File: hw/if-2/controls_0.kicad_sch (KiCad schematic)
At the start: 17 parts, among them Q1 MMBT3904, Q13 2N7002, Q2 MMBT3904

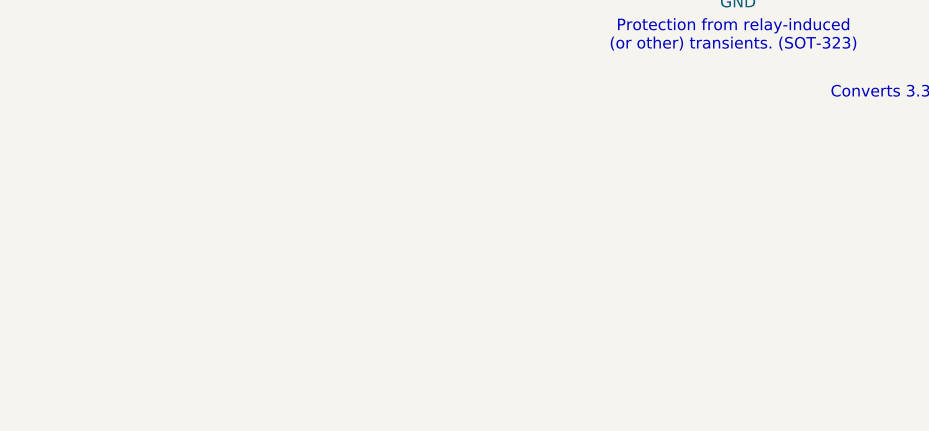
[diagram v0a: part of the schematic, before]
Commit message: Updating schematics, create new mini-board for radio interface
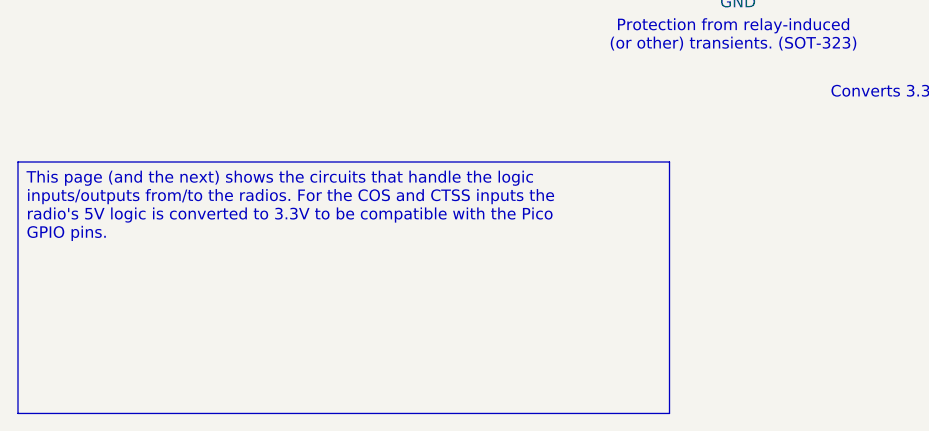
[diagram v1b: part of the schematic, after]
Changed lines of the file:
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@@
 			(font
 				(size 1.27 1.27)
+				(color 255 14 235 1)
 			)
 		)
@@
 			(font
 				(size 1.27 1.27)
+				(color 255 5 238 1)
 			)
 		)
@@
 		)
 	)
+	(text_box "This page (and the next) shows the circuits that handle the logic inputs/outputs from/to the radios. For the COS and CTSS inputs the radio's 5V logic is converted to 3.3V to be compatible with the Pico GPIO pins.\n"
+		(exclude_from_sim no)
+		(at 15.24 171.45 0)
+		(size 72.39 27.94)
+		(margins 0.9525 0.9525 0.9525 0.9525)
+		(stroke
+			(width 0)
+			(type solid)
+		)
+		(fill
+			(type color)
+			(color 205 245 255 1)
+		)
+		(effects
+			(font
+				(size 1.27 1.27)
+			)
+			(justify left top)
+		)
+	)

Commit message: Updating schematics, create new mini-board for radio interface
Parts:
- added R21, R30: 100, Resistor_SMD:R_0805_2012Metric_Pad1.20x1.40mm_HandSolder, symbol Device:R_Small_US
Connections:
- net R0_COS: now also R21.1; no longer C9.1, D6.3 (COM), R24.1, R25.2
- net R0_CTCSS: now also R30.1; no longer C48.1, D7.3 (COM), R27.2, R32.1
- new net: C9.1, D6.3 (COM), R21.2, R24.1, R25.2
- new net: C48.1, D7.3 (COM), R27.2, R30.2, R32.1
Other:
- note added: "When Rx_COS is +5V, base voltage is (5/(10+4.7))*4.7 = 1.6V."
- note added: "When Rx_CTCSS is +5V, base voltage is (5/(10+4.7))*4.7 = 1.6V."
- note removed: "When Rx_COS is +5V, base voltage is 1.6V."
- note removed: "When Rx_CTCSS is +5V, base voltage is 1.6V."
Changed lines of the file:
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@@
 	(title_block
 		(title "COS/CTCSS/PTT Controls (Radio 0)")
-		(date "2025-06-21")
+		(date "2025-06-25")
 		(rev "3")
 		(company "Bruce MacKinnon KC1FSZ")
@@
 		)
 	)
-	(text "When Rx_COS is +5V, base \nvoltage is 1.6V."
-		(exclude_from_sim no)
-		(at 151.13 62.23 0)
-		(effects
-			(font
-				(size 1.27 1.27)
-				(color 255 14 235 1)
-			)
-		)
-	)
-	(text "When Rx_CTCSS is +5V, base \nvoltage is 1.6V."
-		(exclude_from_sim no)
-		(at 151.13 123.19 0)
+	(text "When Rx_CTCSS is +5V, base \nvoltage is (5/(10+4.7))*4.7 = 1.6V.\n"
+		(exclude_from_sim no)
+		(at 153.924 121.92 0)
 		(effects
 			(font
@@
 	(text "Controller Side"
 		(exclude_from_sim no)
-		(at 194.564 88.9 90)
+		(at 201.93 93.98 90)
 		(effects
 			(font
@@
 	(text "Radio Side"
 		(exclude_from_sim no)
-		(at 64.008 84.328 90)
+		(at 46.736 96.266 90)
 		(effects
 			(font
 				(size 5.08 5.08)
+			)
+		)
+	)
+	(text "When Rx_COS is +5V, base \nvoltage is (5/(10+4.7))*4.7 = 1.6V.\n"
+		(exclude_from_sim no)
+		(at 158.75 61.468 0)
+		(effects
+			(font
+				(size 1.27 1.27)
+				(color 255 5 238 1)
 			)
 		)
@@
 	(wire
 		(pts
+			(xy 83.82 107.95) (xy 101.6 107.95)
+		)
+		(stroke
+			(width 0)
+			(type default)
+		)
+	)
+	(wire
+		(pts
 			(xy 95.25 140.97) (xy 121.92 140.97)
 		)
@@
 	(wire
 		(pts
+			(xy 73.66 107.95) (xy 78.74 107.95)
+		)
+		(stroke
+			(width 0)
+			(type default)
+		)
+	)
+	(wire
+		(pts
 			(xy 100.33 26.67) (xy 100.33 46.99)
 		)
@@
 	(wire
 		(pts
-			(xy 100.33 46.99) (xy 90.17 46.99)
-		)
-		(stroke
-			(width 0)
-			(type default)
-		)
-	)
-	(wire
-		(pts
-			(xy 101.6 107.95) (xy 90.17 107.95)
-		)
-		(stroke
-			(width 0)
-			(type default)
-		)
-	)
-	(wire
-		(pts
 			(xy 130.81 46.99) (xy 130.81 49.53)
 		)
@@
 		(pts
 			(xy 105.41 41.91) (xy 105.41 46.99)
+		)
+		(stroke
+			(width 0)
+			(type default)
+		)
+	)
+	(wire
+		(pts
+			(xy 85.09 46.99) (xy 100.33 46.99)
+		)
+		(stroke
+			(width 0)
+			(type default)
+		)
+	)
+	(wire
+		(pts
+			(xy 73.66 46.99) (xy 80.01 46.99)
 		)
 		(stroke
@@
 	(global_label "R0_COS"
 		(shape input)
-		(at 90.17 46.99 180)
+		(at 73.66 46.99 180)
 		(fields_autoplaced yes)
 		(effects
@@
 		)
 		(property "Intersheetrefs" "${INTERSHEET_REFS}"
-			(at 79.9277 46.99 0)
+			(at 63.4177 46.99 0)
 			(effects
 				(font
@@
 	(global_label "R0_CTCSS"
 		(shape input)
-		(at 90.17 107.95 180)
+		(at 73.66 107.95 180)
 		(fields_autoplaced yes)
 		(effects
@@
 		)
 		(property "Intersheetrefs" "${INTERSHEET_REFS}"
-			(at 77.8111 107.95 0)
+			(at 61.3011 107.95 0)
 			(effects
 				(font
@@
 	)
 	(symbol
+		(lib_id "Device:R_Small_US")
+		(at 81.28 107.95 90)
+		(unit 1)
+		(exclude_from_sim no)
+		(in_bom yes)
+		(on_board yes)
+		(dnp no)
+		(fields_autoplaced yes)
+		(property "Reference" "R30"
+			(at 81.28 101.6 90)
+			(effects
+				(font
+					(size 1.27 1.27)
+				)
+			)
+		)
+		(property "Value" "100"
+			(at 81.28 104.14 90)
+			(effects
+				(font
+					(size 1.27 1.27)
+				)
+			)
+		)
+		(property "Footprint" "Resistor_SMD:R_0805_2012Metric_Pad1.20x1.40mm_HandSolder"
+			(at 81.28 107.95 0)
+			(effects
+				(font
+					(size 1.27 1.27)
+				)
+				(hide yes)
+			)
+		)
+		(property "Datasheet" "~"
+			(at 81.28 107.95 0)
+			(effects
+				(font
+					(size 1.27 1.27)
+				)
+				(hide yes)
+			)
+		)
+		(property "Description" "Resistor, small US symbol"
+			(at 81.28 107.95 0)
+			(effects
+				(font
+					(size 1.27 1.27)
+				)
+				(hide yes)
+			)
+		)
+		(pin "2"
+		)
+		(pin "1"
+		)
+		(instances
+			(project "if-2"
+				(path "/a8c2d6aa-29bb-49bd-a367-0d62a0a32480/dfb1fd4a-a237-487e-a7e8-10401a602072"
+					(reference "R30")
+					(unit 1)
+				)
+			)
+		)
+	)
+	(symbol
 		(lib_id "Device:R_US")
 		(at 142.24 148.59 270)
@@
 					(unit 1)
 				)
+			)
+		)
+	)
+	(symbol
+		(lib_id "Device:R_Small_US")
+		(at 82.55 46.99 90)
+		(unit 1)
+		(exclude_from_sim no)
+		(in_bom yes)
+		(on_board yes)
+		(dnp no)
+		(fields_autoplaced yes)
+		(property "Reference" "R21"
+			(at 82.55 40.64 90)
+			(effects
+				(font
+					(size 1.27 1.27)
+				)
+			)
+		)
+		(property "Value" "100"
+			(at 82.55 43.18 90)
+			(effects
+				(font
+					(size 1.27 1.27)
+				)
+			)
+		)
+		(property "Footprint" "Resistor_SMD:R_0805_2012Metric_Pad1.20x1.40mm_HandSolder"
+			(at 82.55 46.99 0)
+			(effects
+				(font
+					(size 1.27 1.27)
+				)
+				(hide yes)
+			)
+		)
+		(property "Datasheet" "~"
+			(at 82.55 46.99 0)
+			(effects
+				(font
+					(size 1.27 1.27)
+				)
+				(hide yes)
+			)
+		)
+		(property "Description" "Resistor, small US symbol"
+			(at 82.55 46.99 0)
+			(effects
+				(font
+					(size 1.27 1.27)
+				)
+				(hide yes)
+			)
+		)
+		(pin "2"
+		)
+		(pin "1"
+		)
+		(instances
+			(project ""
+				(path "/a8c2d6aa-29bb-49bd-a367-0d62a0a32480/dfb1fd4a-a237-487e-a7e8-10401a602072"
+					(reference "R21")
+					(unit 1)
+				)
